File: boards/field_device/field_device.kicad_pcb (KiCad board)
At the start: 4 copper layers, 63 parts, among them J1 Conn_01x05_Pin, J2 Conn_01x02_Pin, SW1 SW_SPST, U1 CHT20MEMS, U2 STM32C011F6Px, U3 SPA06-003, U4 CN3163, U5 HX8001-AJC, U6 SX1262IMLTRT, Y1 Crystal_GND24

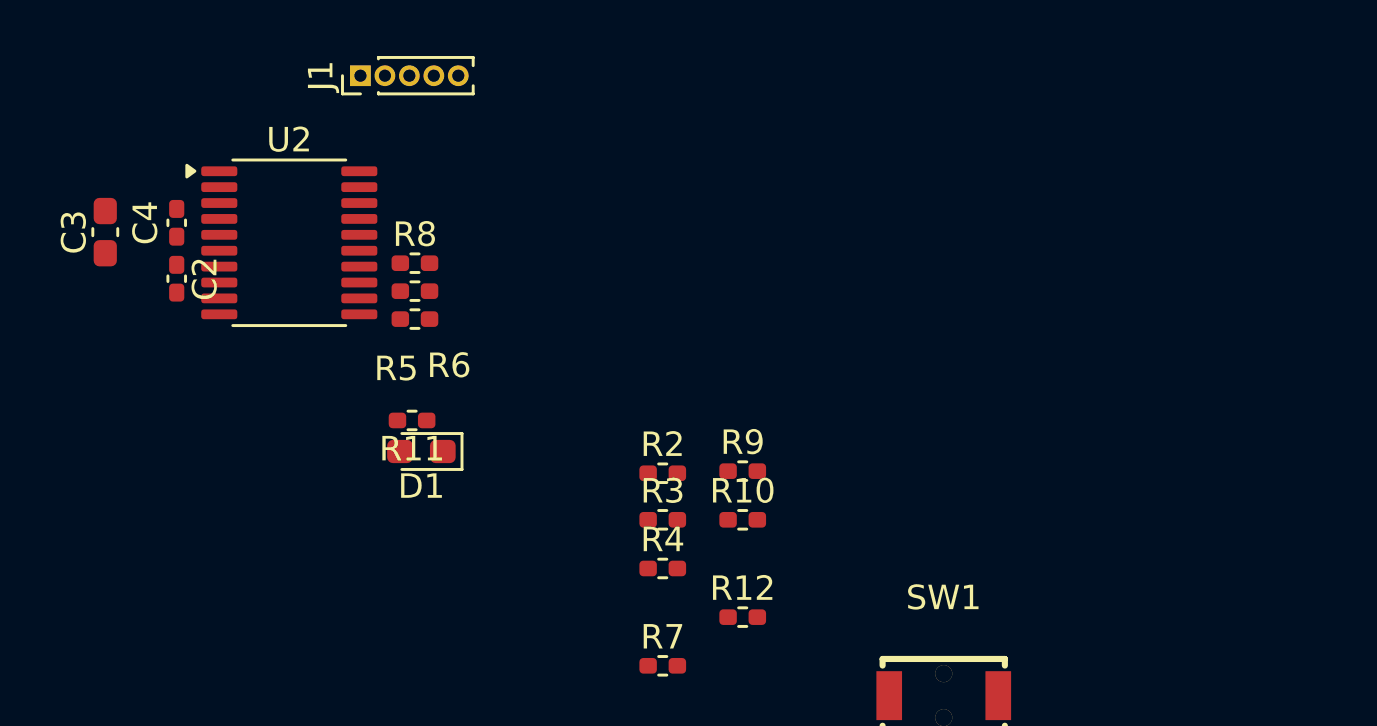
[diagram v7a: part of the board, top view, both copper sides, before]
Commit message: added inductor footprint and did regulator routing
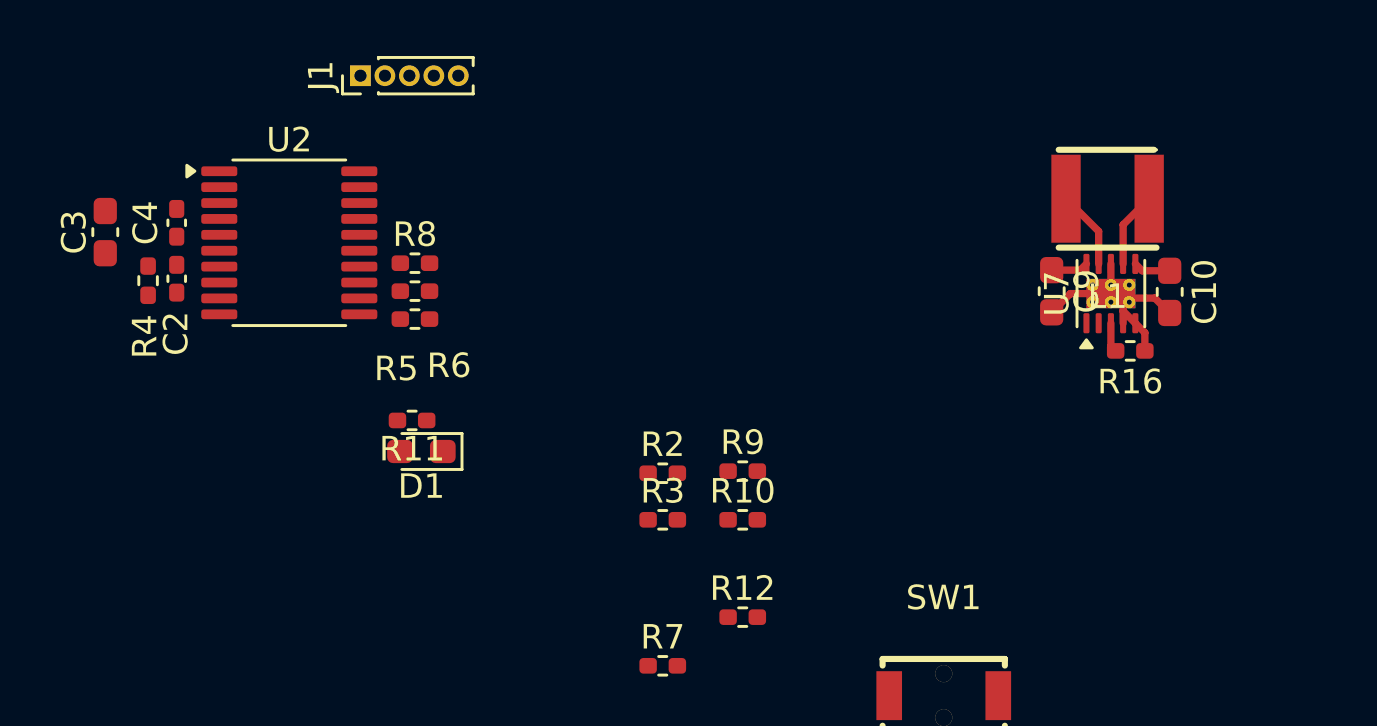
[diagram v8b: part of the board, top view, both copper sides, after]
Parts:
- added C10: 22u, Capacitor_SMD:C_0603_1608Metric_Pad1.08x0.95mm_HandSolder, F.Cu at (182.2, 64.5)
- added C9: 10u, Capacitor_SMD:C_0603_1608Metric_Pad1.08x0.95mm_HandSolder, F.Cu at (177.4, 64.4)
- added L1: 2u2, UnEasy-LCSC:IND-SMD_L4.0-W4.0_B, F.Cu at (179.7, 60.7)
- added R16: 36k5, Resistor_SMD:R_0402_1005Metric_Pad0.72x0.64mm_HandSolder, F.Cu at (180.6, 66.9)
- added U7: TPS63900, Package_SON:WSON-10-1EP_2.5x2.5mm_P0.5mm_EP1.2x2mm_ThermalVias, F.Cu at (179.8, 64.5)
- moved R4 24.1 mm to (140.5, 64.0), turned to 90 degrees
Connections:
- BT1 pad 1: VBUS -> /power_source/regulator/Vin
- C8 pad 1: VBUS -> /power_source/regulator/Vin
- U4 pad 5: VBUS -> /power_source/regulator/Vin
- U4 pad 8: VBUS -> /power_source/regulator/Vin
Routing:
- net GND: track 0.00 -> 9.00 mm
- net /power_source/regulator/LX1: track 0.00 -> 3.22 mm
- net /power_source/regulator/LX2: track 0.00 -> 3.11 mm
- net /power_source/regulator/Vin: track 0.00 -> 1.53 mm
- net +3.3V: track 0.21 -> 1.73 mm
- net /power_source/regulator/CFG1: track 0.00 -> 1.21 mm
